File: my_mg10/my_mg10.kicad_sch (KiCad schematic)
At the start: 127 parts, among them J1 INPUT, J2 PWR_CONN, J3 AUX INPUT, J4 SEND, J5 RETURN, J6 HEADPHONES, K1 G6S-2, SW1 Clean/Overdrive, SW2 FOOTSWITCH, U1 TL072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

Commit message: Minor file tweaks
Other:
- note removed: "TODO: Make it such that when headphones are plugged in, the speaker is not active"
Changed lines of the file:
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@@
-		)
-	)
-	(text "TODO:\nMake it such that when \nheadphones are plugged in,\nthe speaker is not active"
-		(exclude_from_sim no)
-		(at 270.764 135.128 0)
-		(effects
-			(font
-				(size 3 3)
-				(thickness 0.24)
-				(bold yes)
-			)
 		)
 	)

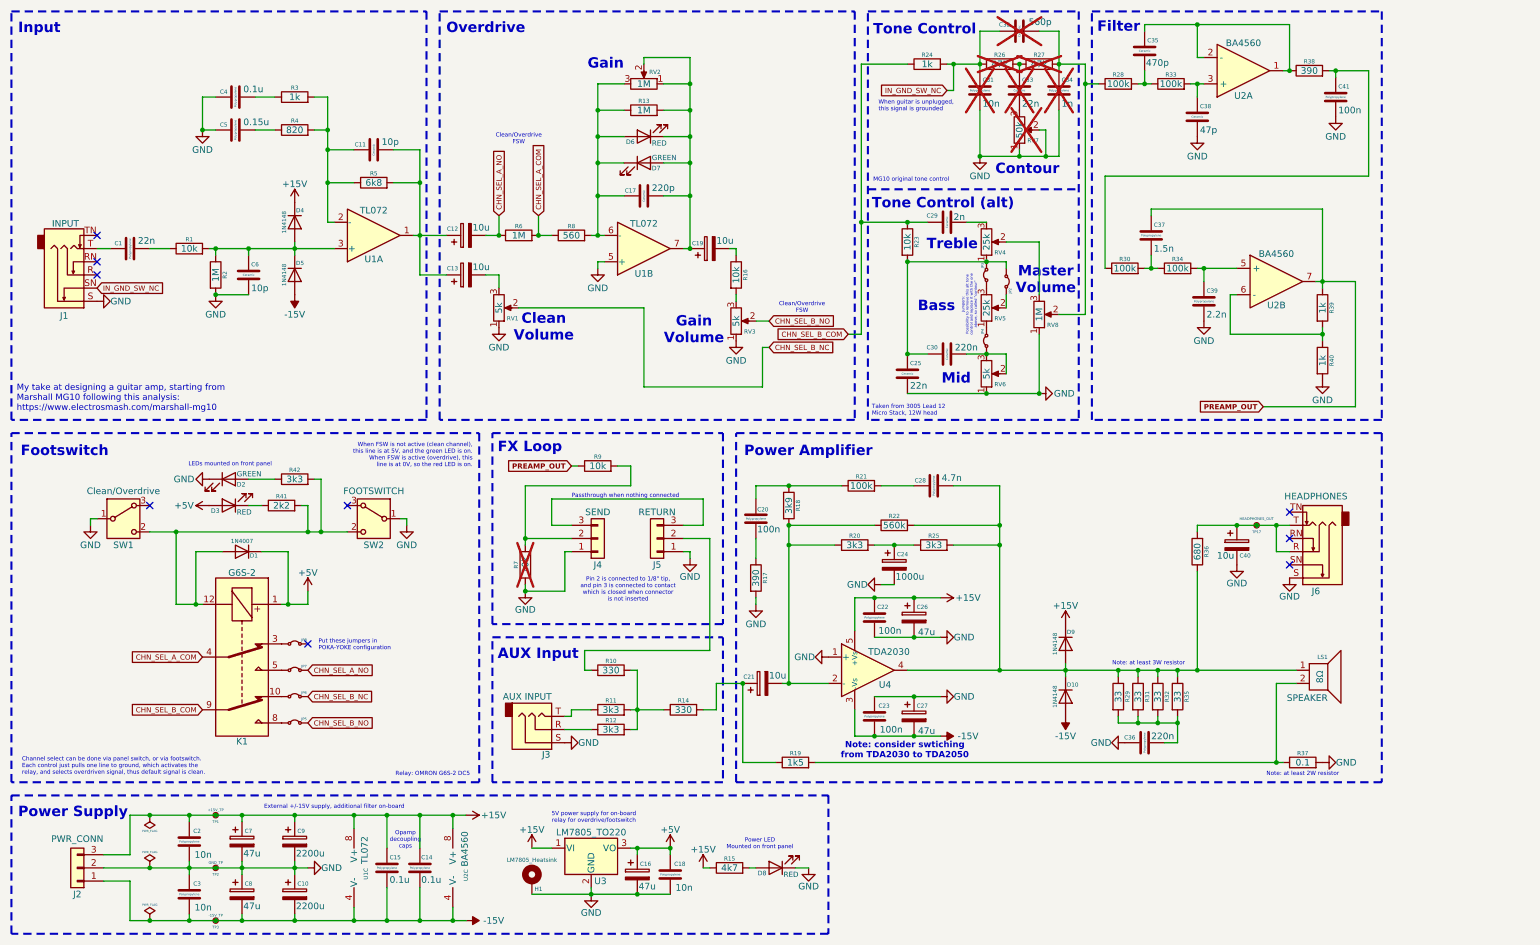
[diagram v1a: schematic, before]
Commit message: Added headphone out switching, added pictures
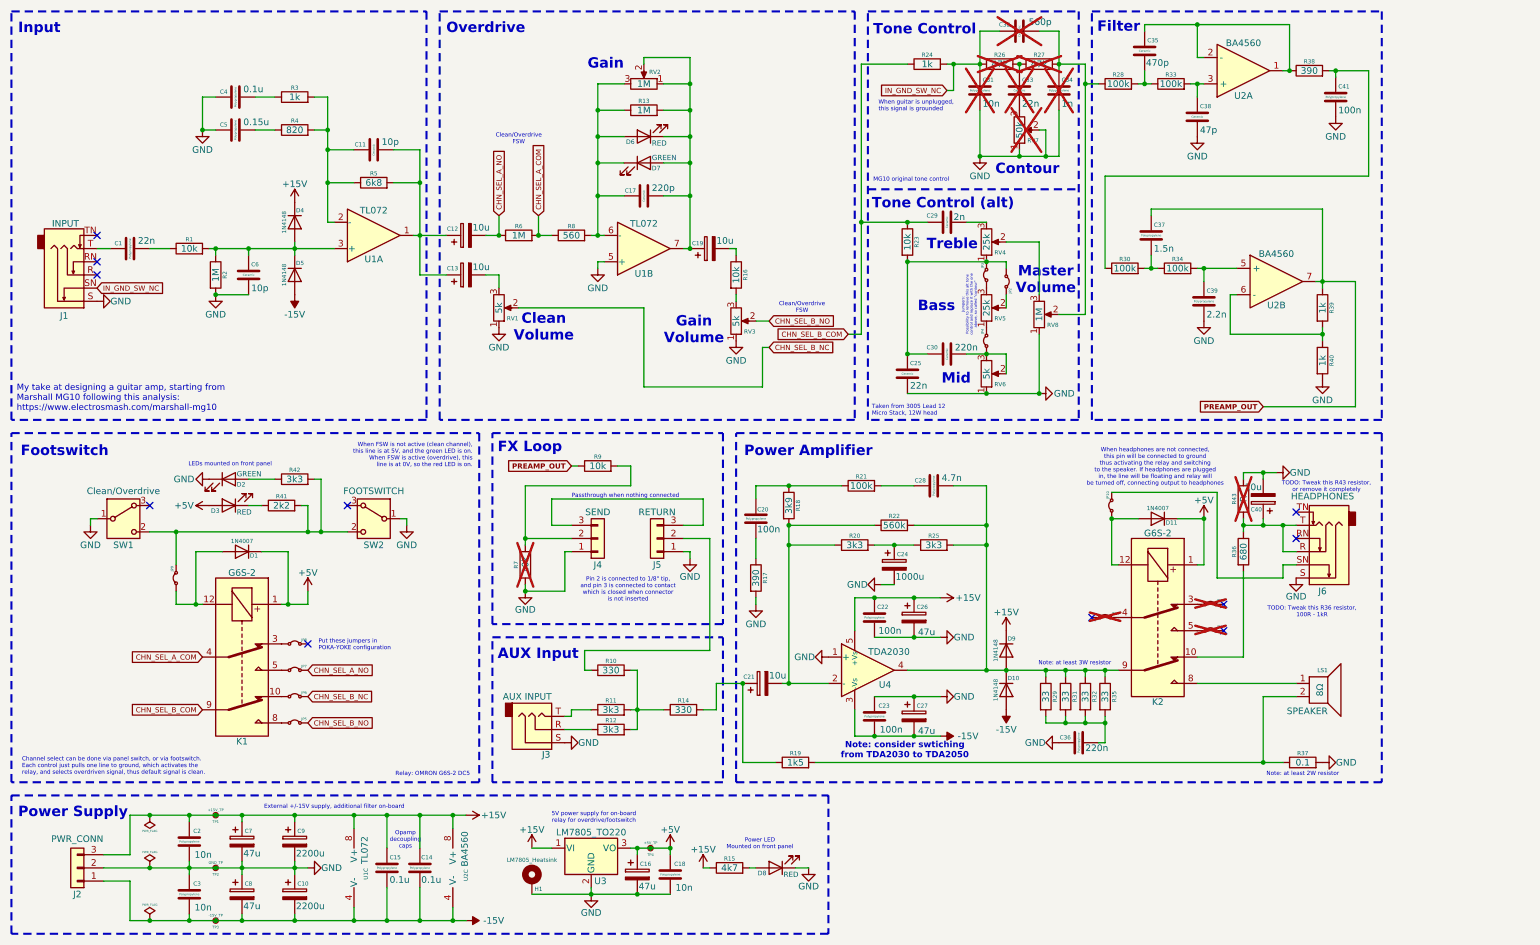
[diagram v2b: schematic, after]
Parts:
- removed TP17: HEADPHONES_OUT, TestPoint:TestPoint_THTPad_D2.5mm_Drill1.2mm, symbol Connector:TestPoint_Small
- added D11: 1N4007, Diode_THT:D_DO-41_SOD81_P10.16mm_Horizontal, symbol Diode:1N4007
- added JP10, JP11, JP12, JP13, JP9: ~, TestPoint:TestPoint_2Pads_Pitch2.54mm_Drill0.8mm, symbol Jumper:Jumper_2_Small_Bridged
- added K2: G6S-2, Relay_THT:Relay_DPDT_Omron_G6S-2, symbol Relay:G6S-2
- added R43: R, Resistor_THT:R_Axial_DIN0207_L6.3mm_D2.5mm_P7.62mm_Horizontal, symbol Device:R
- added TP4: +5V_TP, TestPoint:TestPoint_THTPad_D2.5mm_Drill1.2mm, symbol Connector:TestPoint_Small
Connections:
- net +5V: now also D11.1 (K), K2.1, TP4.1
- net GND: now also R43.2
- net at R41.2, R42.2, SW1.2 (C)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: now also JP9.2 (B); no longer D1.2 (A), K1.12
- net at C28.2, D10.1 (K), D9.2 (A)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: now also K2.9; no longer LS1.1, R36.1
- net at C40.1, J6.R, J6.T: now also R36.1, R43.1; no longer R36.2
- net at J6.SN: now also JP10.2 (B)
- new net: D1.2 (A), JP9.1 (A), K1.12
- new net: K2.10, R36.2
- new net: D11.2 (A), JP10.1 (A), K2.12
- new net: JP12.1 (A), K2.3
- new net: JP11.2 (B), K2.4
- new net: JP13.1 (A), K2.5
- new net: K2.8, LS1.1
- no-connect marks 9 -> 11
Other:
- note added: "TODO: Tweak this R36 resistor, 100R - 1kR"
- note added: "TODO: Tweak this R43 resistor, or remove it completely"
- note added: "When headphones are not connected, this pin will be connected to ground thus activating the relay and switching to the speaker. If headphones are plugged in, the line will be floating and relay will be turned off, connecting output to headphones"
- moved on the sheet: C36, C40, D10, D9, J6, LS1, R29, R31, R32, R35, R36
